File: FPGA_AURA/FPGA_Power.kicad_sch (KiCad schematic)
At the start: 1 part, among them U1 XC7A35T-2FTG256C

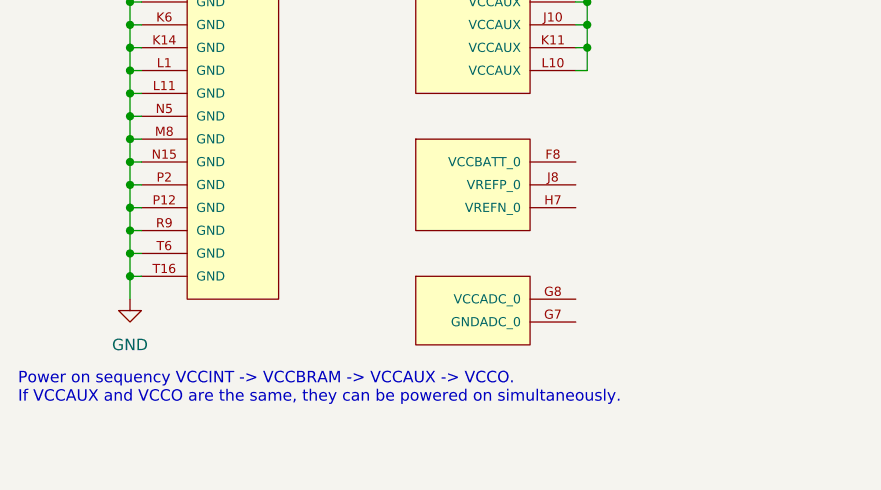
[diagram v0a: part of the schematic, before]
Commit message: Following new DDR3 reference
Using Scopefun v2 as a reference design for the XC7A35T-FTG256
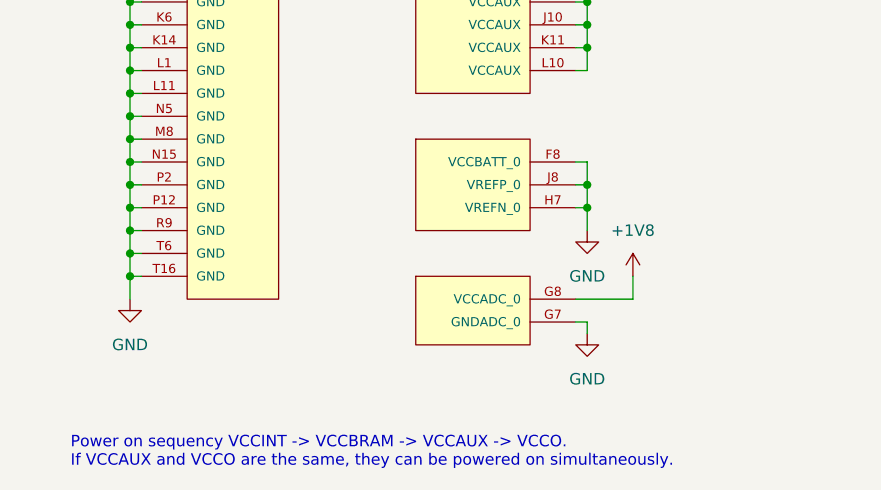
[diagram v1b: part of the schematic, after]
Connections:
- net +1V8: now also U1.G8 (VCCADC_0)
- net GND: now also U1.F8 (VCCBATT_0), U1.G7 (GNDADC_0), U1.H7 (VREFN_0), U1.J8 (VREFP_0)

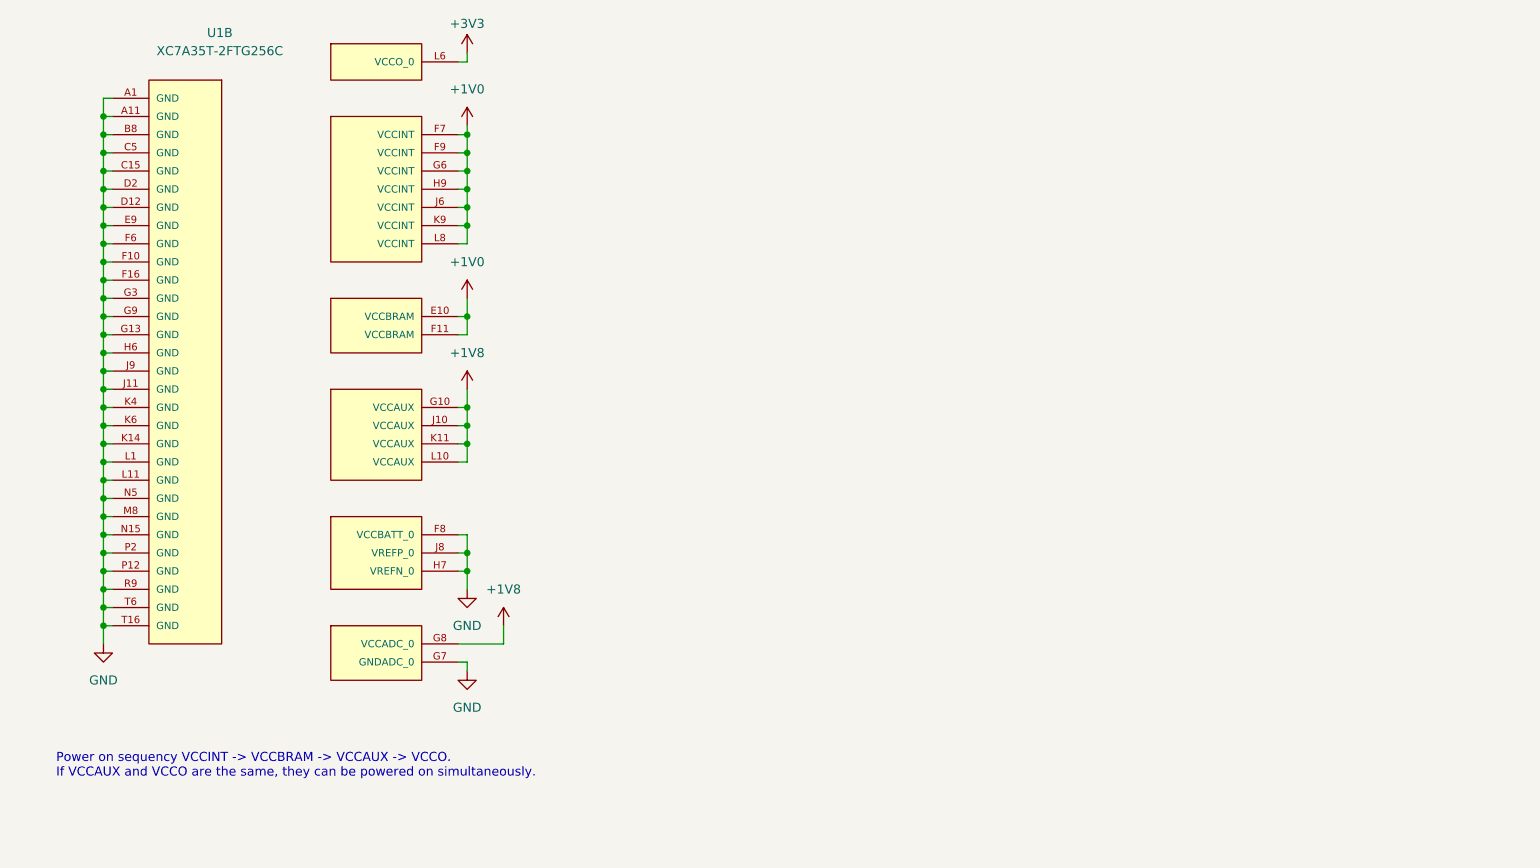
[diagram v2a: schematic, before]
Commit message: Changing stackup to 10 layers and connectors change
Development has been slow due to SI concerns with 8 layers so changing the layer count to 10 will simplify design. The picoblade/SD connector(s) are large and not high speed, so a high speed mezzanine will be used to go to a daughter board with the picoblade connectors and SD card, or other devices/protocols e.g. ADCs, COAX, IMUs, etc.
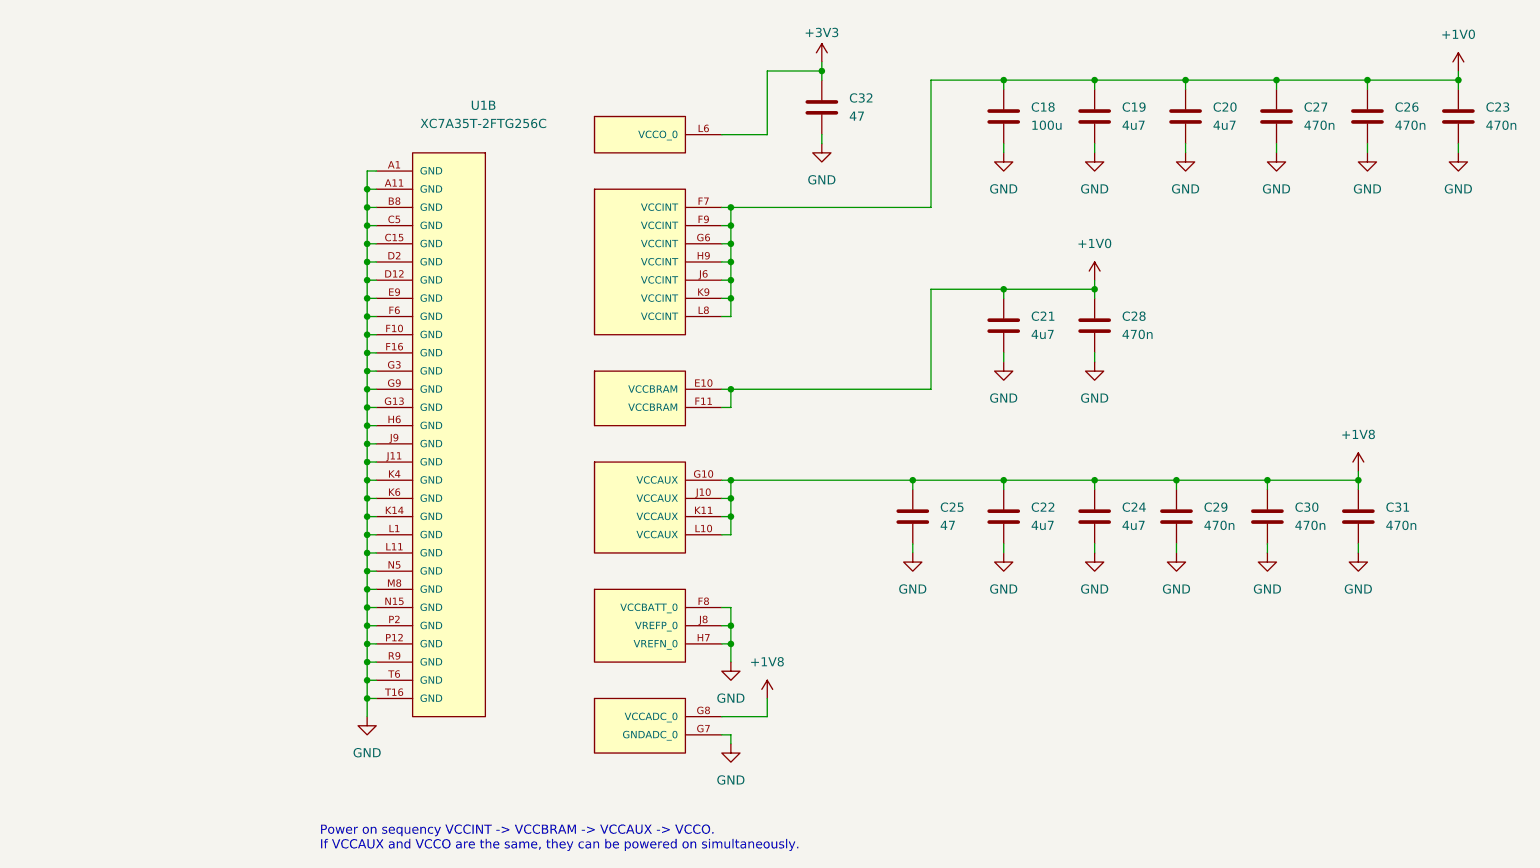
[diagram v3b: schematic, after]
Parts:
- added C18: 100u, Capacitor_SMD:C_0805_2012Metric, symbol Device:C
- added C19, C20, C21, C22, C24: 4u7, Capacitor_SMD:C_0603_1608Metric, symbol Device:C
- added C23, C26, C27, C28, C29, C30, C31: 470n, Capacitor_SMD:C_0402_1005Metric, symbol Device:C
- added C25, C32: 47, Capacitor_SMD:C_0603_1608Metric, symbol Device:C
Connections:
- net +1V0: now also C18.1, C19.1, C20.1, C21.1, C23.1, C26.1, C27.1, C28.1
- net +1V8: now also C22.1, C24.1, C25.1, C29.1, C30.1, C31.1
- net +3V3: now also C32.1
- net GND: now also C18.2, C19.2, C20.2, C21.2, C22.2, C23.2, C24.2, C25.2, C26.2, C27.2, C28.2, C29.2, C30.2, C31.2, C32.2
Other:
- moved on the sheet: U1B
